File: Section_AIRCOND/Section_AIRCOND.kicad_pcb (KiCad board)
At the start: 2 copper layers, 150.5 x 39 mm, 46 parts, among them J1 AIRCOND ribbon, J2 Backlight, SW1 AIRCOND APU BLEED, SW2 AIRCOND PACK 1, SW3 AIRCOND PACK 2, SW4 AIRCOND EXT PWR

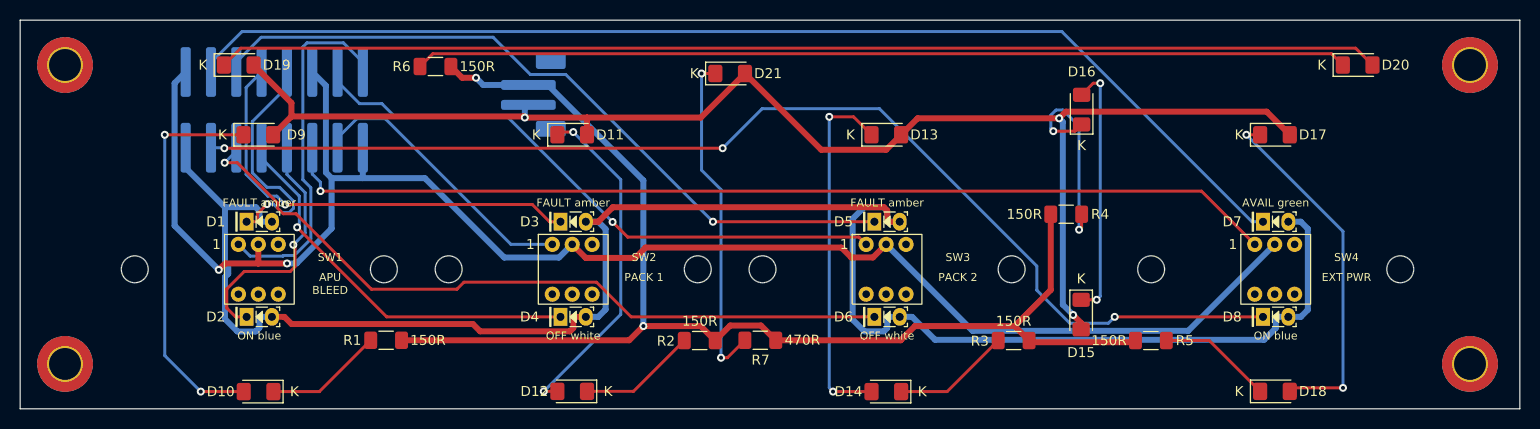
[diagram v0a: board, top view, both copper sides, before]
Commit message: Single-LED backlight strings on 330 ohm, not 470
A pair of backlight LEDs on 150 ohm runs at 17 mA (Stefano's figure). The
470 ohm came from an estimated 11 mA per string, which was wrong. For the
same 17 mA a single LED needs V / (2 I) + 75 ohm = 330 ohm. Changed on APU
(R3), GPWS (R5), AIR COND (R7, the v1 R76) and EXT LT (R16); the document's
backlight currents now use 17 mA, ~1.1 A in all. The four boards rebuilt
and rerouted: ERC 0, DRC 0, nothing unconnected, no parity issues.

Co-Authored-By: Claude Opus 5.5 <noreply@anthropic.com>
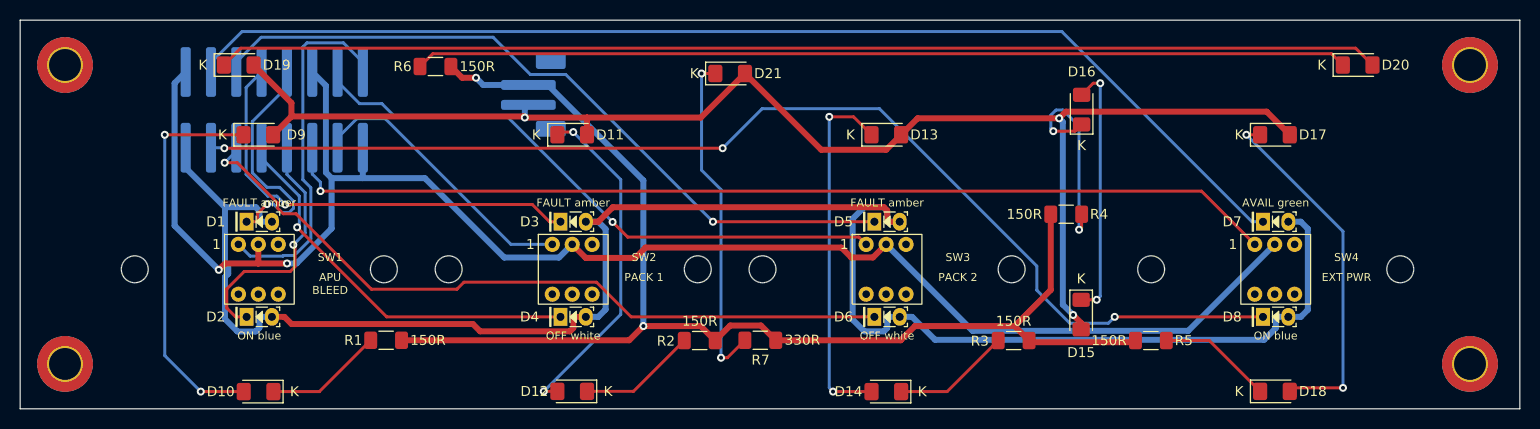
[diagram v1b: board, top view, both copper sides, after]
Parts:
- R7: value 470 -> 330
